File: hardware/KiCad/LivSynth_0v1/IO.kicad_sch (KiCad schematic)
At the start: 88 parts, among them J13 Jumper, J14 PJ398SM, J15 Molex, J16 Molex, J17 Jumper, J18 PJ398SM, J19 PJ398SM, Q15 2N3904, Q16 2N3904, SW7 SW_Push, U16 PCA9685PW, U17 PCA9685PW, U18 74HC165, U19 74HC165, U20 LM386

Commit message: Initial Routing finished
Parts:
- added D11: LED_RKGB, LED_THT:LED_D5.0mm-4_RGB, symbol Device:LED_RKGB
- added NT3, NT4, NT5: NetTie_2, NetTie:NetTie-2_SMD_Pad2.0mm, symbol Device:NetTie_2
- added R127, R128, R129: 220R, Resistor_THT:R_Axial_DIN0207_L6.3mm_D2.5mm_P7.62mm_Horizontal, symbol Device:R_Small
- C51: symbol Device:C_Polarized_Small -> Device:C_Small
- J14, J18, J19: footprint (none) -> SloBlo:Thonkiconn_PJ398SM
- J15: value Molex -> IDC; footprint (none) -> Connector_PinHeader_2.54mm:PinHeader_1x02_P2.54mm_Vertical
- J16: value Molex -> IDC
- RGB_Pot1, RGB_Pot2, RGB_Pot3, RGB_Pot4: footprint (none) -> SloBlo:TC002-N11AS2XT-RGB
- RGB_Pot5: renamed from RGB_Pot7; footprint (none) -> SloBlo:TC002-N11AS2XT-RGB
- RGB_Pot6: renamed from RGB_Pot8; footprint (none) -> SloBlo:TC002-N11AS2XT-RGB
- RGB_Pot7: renamed from RGB_Pot9; footprint (none) -> SloBlo:TC002-N11AS2XT-RGB
- RGB_Pot8: renamed from RGB_Pot5; footprint (none) -> SloBlo:TC002-N11AS2XT-RGB
- RGB_Pot9: renamed from RGB_Pot6; footprint (none) -> SloBlo:TC002-N11AS2XT-RGB
- RV19, RV21: footprint (none) -> SloBlo:Alpha_RD901F
- RV20: footprint (none) -> SloBlo:RV141F-40-20BL
- SW7: footprint (none) -> SloBlo:E-Switch_TL1105SP
- U18, U19: footprint (none) -> Package_SO:SOIC-16_3.9x9.9mm_P1.27mm
- U20: footprint (none) -> Package_DIP:DIP-8_W7.62mm_Socket
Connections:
- net GND: now also D11.2 (K), NT3.1, NT4.2, NT5.1; no longer J14.1, J18.1, J19.1
- net LED1_B: now also R129.2
- net LED1_G: now also R128.2
- net LED1_R: now also R127.2
- net ADC_OUT1 renamed ADC_IN1
- net ADC_OUT2 renamed ADC_IN2
- net CLOCK_IN renamed CLOCK_OUT
- net RESET_IN renamed RESET_OUT
- new net: D11.4 (BA), R129.1
- new net: D11.1 (RA), R127.1
- new net: J19.1, NT5.2
- new net: J18.1, NT4.1
- new net: J14.1, NT3.2
- new net: D11.3 (GA), R128.1
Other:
- note added: "External"

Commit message: Rework for polyester film capacitors
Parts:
- C42, C43, C44, C45, C51, C54, C55: footprint Capacitor_THT:C_Disc_D3.0mm_W1.6mm_P2.50mm -> Capacitor_THT:C_Rect_L7.2mm_W2.5mm_P5.00mm_FKS2_FKP2_MKS2_MKP2
- C46: footprint Capacitor_THT:C_Disc_D3.0mm_W1.6mm_P2.50mm -> Capacitor_THT:C_Rect_L7.2mm_W5.5mm_P5.00mm_FKS2_FKP2_MKS2_MKP2
- C47, C49, C53: footprint Capacitor_THT:C_Disc_D3.0mm_W1.6mm_P2.50mm -> Capacitor_THT:C_Rect_L7.2mm_W4.5mm_P5.00mm_FKS2_FKP2_MKS2_MKP2
- J16, LS1: footprint (none) -> Capacitor_THT:C_Rect_L7.2mm_W2.5mm_P5.00mm_FKS2_FKP2_MKS2_MKP2
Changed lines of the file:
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@@
     (property "Reference" "C46" (id 0) (at 343.6239 24.13 90))
     (property "Value" "1u" (id 1) (at 343.6239 26.67 90))
-    (property "Footprint" "Capacitor_THT:C_Disc_D3.0mm_W1.6mm_P2.50mm" (id 2) (at 344.17 31.115 0)
+    (property "Footprint" "Capacitor_THT:C_Rect_L7.2mm_W5.5mm_P5.00mm_FKS2_FKP2_MKS2_MKP2" (id 2) (at 344.17 31.115 0)
       (effects (font (size 1.27 1.27)) hide)
     )
@@
       (effects (font (size 1.27 1.27)) (justify left))
     )
-    (property "Footprint" "Capacitor_THT:C_Disc_D3.0mm_W1.6mm_P2.50mm" (id 2) (at 227.33 28.575 0)
+    (property "Footprint" "Capacitor_THT:C_Rect_L7.2mm_W2.5mm_P5.00mm_FKS2_FKP2_MKS2_MKP2" (id 2) (at 227.33 28.575 0)
       (effects (font (size 1.27 1.27)) hide)
     )
@@
       (effects (font (size 1.27 1.27)) (justify left))
     )
-    (property "Footprint" "Capacitor_THT:C_Disc_D3.0mm_W1.6mm_P2.50mm" (id 2) (at 118.745 24.13 0)
+    (property "Footprint" "Capacitor_THT:C_Rect_L7.2mm_W2.5mm_P5.00mm_FKS2_FKP2_MKS2_MKP2" (id 2) (at 118.745 24.13 0)
       (effects (font (size 1.27 1.27)) hide)
     )
@@
       (effects (font (size 1.27 1.27)) (justify right))
     )
-    (property "Footprint" "Capacitor_THT:C_Disc_D3.0mm_W1.6mm_P2.50mm" (id 2) (at 326.39 73.66 0)
+    (property "Footprint" "Capacitor_THT:C_Rect_L7.2mm_W4.5mm_P5.00mm_FKS2_FKP2_MKS2_MKP2" (id 2) (at 326.39 73.66 0)
       (effects (font (size 1.27 1.27)) hide)
     )
@@
       (effects (font (size 1.27 1.27)) (justify left))
     )
-    (property "Footprint" "Capacitor_THT:C_Disc_D3.0mm_W1.6mm_P2.50mm" (id 2) (at 52.705 24.13 0)
+    (property "Footprint" "Capacitor_THT:C_Rect_L7.2mm_W2.5mm_P5.00mm_FKS2_FKP2_MKS2_MKP2" (id 2) (at 52.705 24.13 0)
       (effects (font (size 1.27 1.27)) hide)
     )
@@
     (property "Reference" "C49" (id 0) (at 313.6963 57.15 90))
     (property "Value" "270n" (id 1) (at 313.6963 59.69 90))
-    (property "Footprint" "Capacitor_THT:C_Disc_D3.0mm_W1.6mm_P2.50mm" (id 2) (at 313.69 64.135 0)
+    (property "Footprint" "Capacitor_THT:C_Rect_L7.2mm_W4.5mm_P5.00mm_FKS2_FKP2_MKS2_MKP2" (id 2) (at 313.69 64.135 0)
       (effects (font (size 1.27 1.27)) hide)
     )
@@
       (effects (font (size 1.27 1.27)) (justify left))
     )
-    (property "Footprint" "" (id 2) (at 387.35 71.755 0)
+    (property "Footprint" "Capacitor_THT:C_Rect_L7.2mm_W2.5mm_P5.00mm_FKS2_FKP2_MKS2_MKP2" (id 2) (at 387.35 71.755 0)
       (effects (font (size 1.27 1.27)) hide)
     )
@@
       (effects (font (size 1.27 1.27)) (justify left))
     )
-    (property "Footprint" "Capacitor_THT:C_Disc_D3.0mm_W1.6mm_P2.50mm" (id 2) (at 327.025 53.975 0)
+    (property "Footprint" "Capacitor_THT:C_Rect_L7.2mm_W4.5mm_P5.00mm_FKS2_FKP2_MKS2_MKP2" (id 2) (at 327.025 53.975 0)
       (effects (font (size 1.27 1.27)) hide)
     )
@@
       (effects (font (size 1.27 1.27)) (justify left))
     )
-    (property "Footprint" "Capacitor_THT:C_Disc_D3.0mm_W1.6mm_P2.50mm" (id 2) (at 63.5 187.325 0)
+    (property "Footprint" "Capacitor_THT:C_Rect_L7.2mm_W2.5mm_P5.00mm_FKS2_FKP2_MKS2_MKP2" (id 2) (at 63.5 187.325 0)
       (effects (font (size 1.27 1.27)) hide)
     )
@@
     (property "Reference" "J16" (id 0) (at 375.92 60.325 0))
     (property "Value" "IDC" (id 1) (at 375.92 62.865 0))
-    (property "Footprint" "" (id 2) (at 373.38 66.675 0)
+    (property "Footprint" "Capacitor_THT:C_Rect_L7.2mm_W2.5mm_P5.00mm_FKS2_FKP2_MKS2_MKP2" (id 2) (at 373.38 66.675 0)
       (effects (font (size 1.27 1.27)) hide)
     )
@@
       (effects (font (size 1.27 1.27)) (justify left))
     )
-    (property "Footprint" "Capacitor_THT:C_Disc_D3.0mm_W1.6mm_P2.50mm" (id 2) (at 31.75 187.325 0)
+    (property "Footprint" "Capacitor_THT:C_Rect_L7.2mm_W2.5mm_P5.00mm_FKS2_FKP2_MKS2_MKP2" (id 2) (at 31.75 187.325 0)
       (effects (font (size 1.27 1.27)) hide)
     )
@@
       (effects (font (size 1.27 1.27)) (justify left))
     )
-    (property "Footprint" "Capacitor_THT:C_Disc_D3.0mm_W1.6mm_P2.50mm" (id 2) (at 351.79 71.12 0)
+    (property "Footprint" "Capacitor_THT:C_Rect_L7.2mm_W2.5mm_P5.00mm_FKS2_FKP2_MKS2_MKP2" (id 2) (at 351.79 71.12 0)
       (effects (font (size 1.27 1.27)) hide)
     )
@@
       (effects (font (size 1.27 1.27)) (justify left))
     )
-    (property "Footprint" "Capacitor_THT:C_Disc_D3.0mm_W1.6mm_P2.50mm" (id 2) (at 180.34 28.575 0)
-      (effects (font (size 1.27 1.27)) hide)
-    )
+    (property "Footprint" "Capacitor_THT:C_Rect_L7.2mm_W2.5mm_P5.00mm_FKS2_FKP2_MKS2_MKP2" (id 2) (at 180.34 28.575 0)
+      (effects (font (size 1.27 1.27)) hide)
+    )

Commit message: Change LED status circuits
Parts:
- J16, LS1: footprint Capacitor_THT:C_Rect_L7.2mm_W2.5mm_P5.00mm_FKS2_FKP2_MKS2_MKP2 -> (none)
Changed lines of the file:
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@@
       (effects (font (size 1.27 1.27)) (justify left))
     )
-    (property "Footprint" "Capacitor_THT:C_Rect_L7.2mm_W2.5mm_P5.00mm_FKS2_FKP2_MKS2_MKP2" (id 2) (at 387.35 71.755 0)
+    (property "Footprint" "" (id 2) (at 387.35 71.755 0)
       (effects (font (size 1.27 1.27)) hide)
     )
@@
     (property "Reference" "J16" (id 0) (at 375.92 60.325 0))
     (property "Value" "IDC" (id 1) (at 375.92 62.865 0))
-    (property "Footprint" "Capacitor_THT:C_Rect_L7.2mm_W2.5mm_P5.00mm_FKS2_FKP2_MKS2_MKP2" (id 2) (at 373.38 66.675 0)
-      (effects (font (size 1.27 1.27)) hide)
-    )
+    (property "Footprint" "" (id 2) (at 373.38 66.675 0)
+      (effects (font (size 1.27 1.27)) hide)
+    )

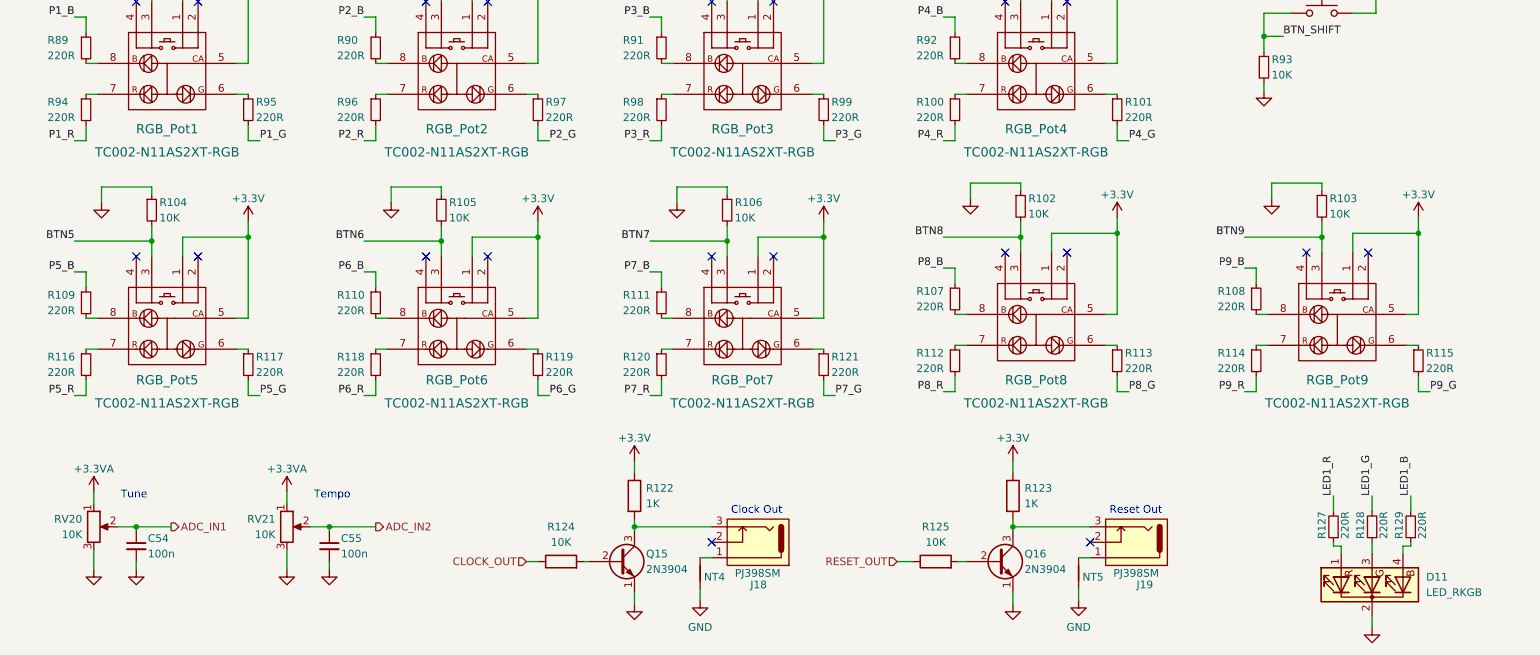
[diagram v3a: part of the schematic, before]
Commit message: White balance for RGB LEDs
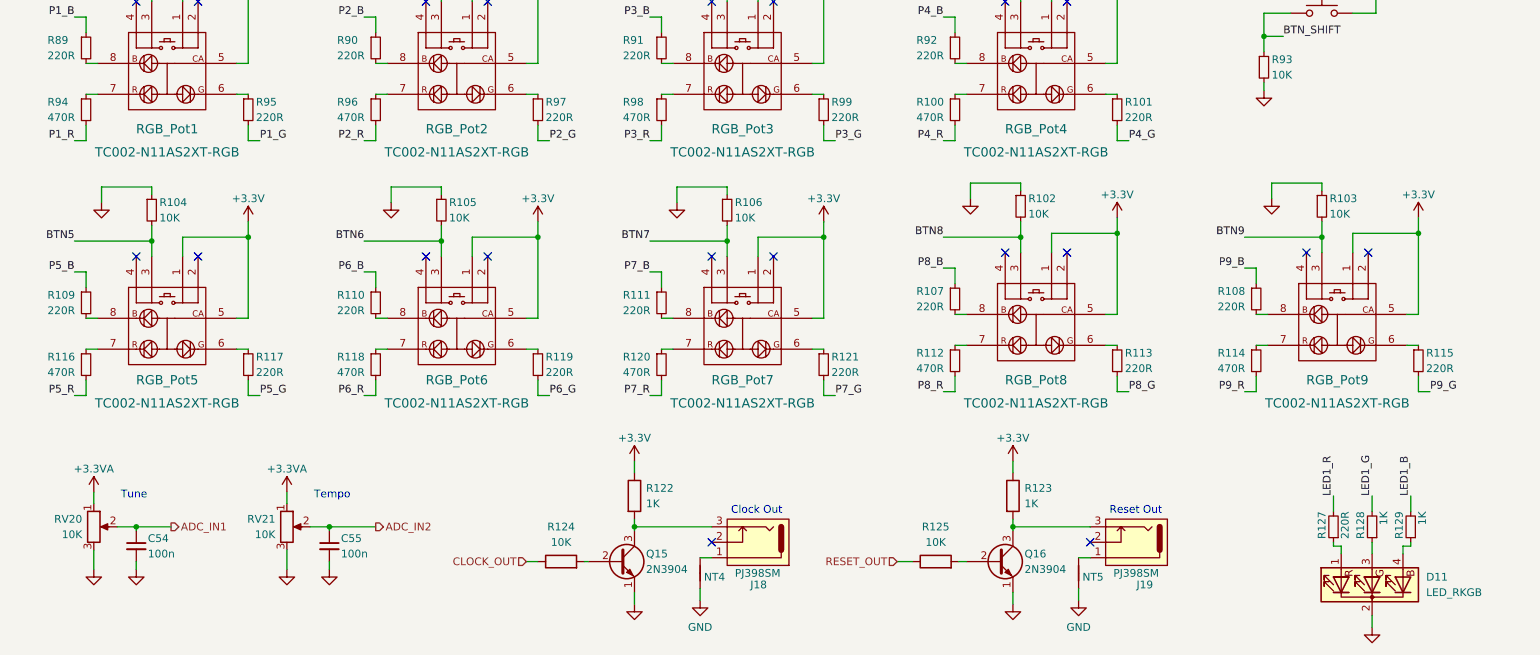
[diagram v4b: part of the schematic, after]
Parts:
- R100, R112, R114, R116, R118, R120, R94, R96, R98: value 220R -> 470R
- R128, R129: value 220R -> 1K
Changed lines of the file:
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@@
       (effects (font (size 1.27 1.27)) (justify left))
     )
-    (property "Value" "220R" (id 1) (at 243.205 181.61 90)
+    (property "Value" "1K" (id 1) (at 243.205 181.61 90)
       (effects (font (size 1.27 1.27)) (justify left))
     )
@@
       (effects (font (size 1.27 1.27)) (justify left))
     )
-    (property "Value" "220R" (id 1) (at 111.76 158.75 0)
+    (property "Value" "470R" (id 1) (at 111.76 158.75 0)
       (effects (font (size 1.27 1.27)) (justify left))
     )
@@
       (effects (font (size 1.27 1.27)) (justify left))
     )
-    (property "Value" "220R" (id 1) (at 209.55 158.115 0)
+    (property "Value" "470R" (id 1) (at 209.55 158.115 0)
       (effects (font (size 1.27 1.27)) (justify left))
     )
@@
       (effects (font (size 1.27 1.27)) (justify left))
     )
-    (property "Value" "220R" (id 1) (at 111.76 116.84 0)
+    (property "Value" "470R" (id 1) (at 111.76 116.84 0)
       (effects (font (size 1.27 1.27)) (justify left))
     )
@@
       (effects (font (size 1.27 1.27)) (justify left))
     )
-    (property "Value" "220R" (id 1) (at 17.145 116.84 0)
+    (property "Value" "470R" (id 1) (at 17.145 116.84 0)
       (effects (font (size 1.27 1.27)) (justify left))
     )
@@
       (effects (font (size 1.27 1.27)) (justify left))
     )
-    (property "Value" "220R" (id 1) (at 64.77 116.84 0)
+    (property "Value" "470R" (id 1) (at 64.77 116.84 0)
       (effects (font (size 1.27 1.27)) (justify left))
     )
@@
       (effects (font (size 1.27 1.27)) (justify left))
     )
-    (property "Value" "220R" (id 1) (at 64.77 158.75 0)
+    (property "Value" "470R" (id 1) (at 64.77 158.75 0)
       (effects (font (size 1.27 1.27)) (justify left))
     )
@@
       (effects (font (size 1.27 1.27)) (justify left))
     )
-    (property "Value" "220R" (id 1) (at 160.02 116.84 0)
+    (property "Value" "470R" (id 1) (at 160.02 116.84 0)
       (effects (font (size 1.27 1.27)) (justify left))
     )
@@
       (effects (font (size 1.27 1.27)) (justify left))
     )
-    (property "Value" "220R" (id 1) (at 160.02 158.115 0)
+    (property "Value" "470R" (id 1) (at 160.02 158.115 0)
       (effects (font (size 1.27 1.27)) (justify left))
     )
@@
       (effects (font (size 1.27 1.27)) (justify left))
     )
-    (property "Value" "220R" (id 1) (at 17.145 158.75 0)
+    (property "Value" "470R" (id 1) (at 17.145 158.75 0)
       (effects (font (size 1.27 1.27)) (justify left))
     )
@@
       (effects (font (size 1.27 1.27)) (justify left))
     )
-    (property "Value" "220R" (id 1) (at 236.855 181.61 90)
-      (effects (font (size 1.27 1.27)) (justify left))
-    )
+    (property "Value" "1K" (id 1) (at 236.855 181.61 90)
+      (effects (font (size 1.27 1.27)) (justify left))
+    )

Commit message: Use correct Elko sizes (8mm/3.5mm)
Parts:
- C48, C50: footprint Capacitor_THT:CP_Radial_D8.0mm_P5.00mm -> Capacitor_THT:CP_Radial_D8.0mm_P3.50mm
- J16, LS1: footprint (none) -> Capacitor_THT:CP_Radial_D8.0mm_P3.50mm
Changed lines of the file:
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@@
       (effects (font (size 1.27 1.27)) (justify left))
     )
-    (property "Footprint" "Capacitor_THT:CP_Radial_D8.0mm_P5.00mm" (id 2) (at 342.265 55.245 0)
+    (property "Footprint" "Capacitor_THT:CP_Radial_D8.0mm_P3.50mm" (id 2) (at 342.265 55.245 0)
       (effects (font (size 1.27 1.27)) hide)
     )
@@
       (effects (font (size 1.27 1.27)) (justify left))
     )
-    (property "Footprint" "" (id 2) (at 387.35 71.755 0)
+    (property "Footprint" "Capacitor_THT:CP_Radial_D8.0mm_P3.50mm" (id 2) (at 387.35 71.755 0)
       (effects (font (size 1.27 1.27)) hide)
     )
@@
     (property "Reference" "J16" (id 0) (at 375.92 60.325 0))
     (property "Value" "IDC" (id 1) (at 375.92 62.865 0))
-    (property "Footprint" "" (id 2) (at 373.38 66.675 0)
+    (property "Footprint" "Capacitor_THT:CP_Radial_D8.0mm_P3.50mm" (id 2) (at 373.38 66.675 0)
       (effects (font (size 1.27 1.27)) hide)
     )
@@
     (property "Reference" "C50" (id 0) (at 359.4989 59.69 90))
     (property "Value" "470u" (id 1) (at 359.4989 62.23 90))
-    (property "Footprint" "Capacitor_THT:CP_Radial_D8.0mm_P5.00mm" (id 2) (at 360.045 66.675 0)
-      (effects (font (size 1.27 1.27)) hide)
-    )
+    (property "Footprint" "Capacitor_THT:CP_Radial_D8.0mm_P3.50mm" (id 2) (at 360.045 66.675 0)
+      (effects (font (size 1.27 1.27)) hide)
+    )

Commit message: 0v1 Ready for Production
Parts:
- renumbered C52 to C19, C46 to C2, C47 to C21, C50 to C22, C45 to C38, C44 to C42, C54 to C5, C55 to C52, C43 to C53, C42 to C54, C53 to C6, C49 to C7, C48 to C8, C51 to C9, D11 to D5, J14 to J1, J13 to J10, J17 to J11, J18 to J2, J19 to J3, J15 to J4, NT3 to NT1, NT5 to NT3, Q16 to Q3, Q15 to Q4, R127 to R10, R105 to R100, R117 to R101, R101 to R102, R104 to R103, R88 to R104, R87 to R105, R99 to R106, R97 to R107, R86 to R108, R85 to R109, R95 to R110, R80 to R111, R81 to R112, R107 to R113, R112 to R114, R111 to R115, R118 to R116, R120 to R117, R110 to R118, R116 to R119, R100 to R120, R109 to R121, R92 to R122, R98 to R123, R91 to R124, R96 to R125, R90 to R126, R89 to R127, R94 to R128, R123 to R13, R125 to R14, R122 to R15, R124 to R16, R82 to R33, R83 to R34, R84 to R59, R115 to R79, R128 to R8, R108 to R80, R114 to R81, R103 to R82, R129 to R9, R102 to R94, R113 to R95, R119 to R96, R93 to R97, R106 to R98, R121 to R99, RGB_Pot9 to RGB_Pot1, RGB_Pot1 to RGB_Pot2, RGB_Pot2 to RGB_Pot3, RGB_Pot3 to RGB_Pot4, RGB_Pot4 to RGB_Pot5, RGB_Pot5 to RGB_Pot6, RGB_Pot6 to RGB_Pot8, RGB_Pot8 to RGB_Pot9, RV20 to RV1, RV21 to RV22, RV19 to RV6, SW7 to SW5, U19 to U10, U17 to U11, U16 to U12, U18 to U13, U20 to U2
